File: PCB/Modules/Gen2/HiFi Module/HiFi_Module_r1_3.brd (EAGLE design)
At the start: 78.7 x 56.5 mm, 22 parts, among them IC1 SN65HVD31DR, IC2 ADUM5200ARWZ, T4_1 TEENSY4.1_FORAUDIO

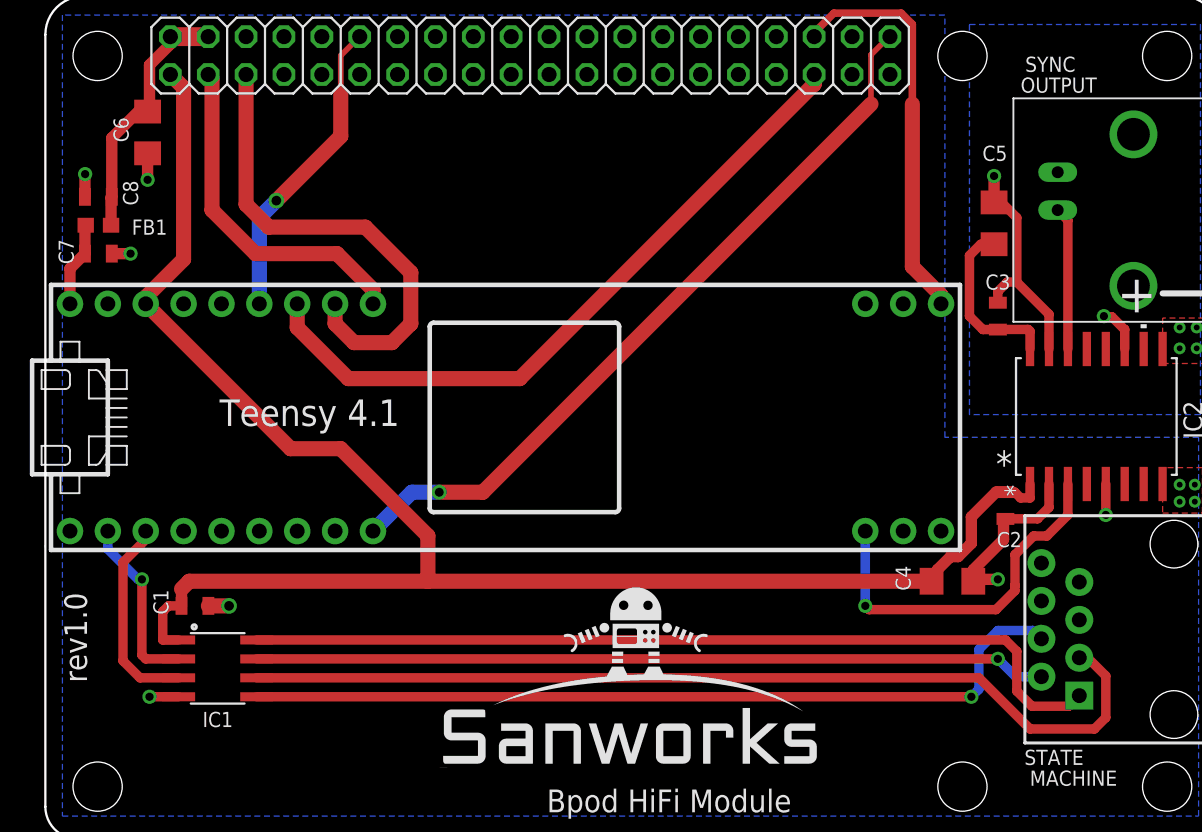
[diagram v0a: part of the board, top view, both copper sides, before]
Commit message: -Updated HiFi module PCB to v1.3. New version pulls unused channel to GND on ADUM5200 isolator, and contains silkscreen instructions for header mounting -Updated Raspberry Pi Shim to v1.1. New version provides more space between RJ45 jack and RS-485 IC for even mounting.
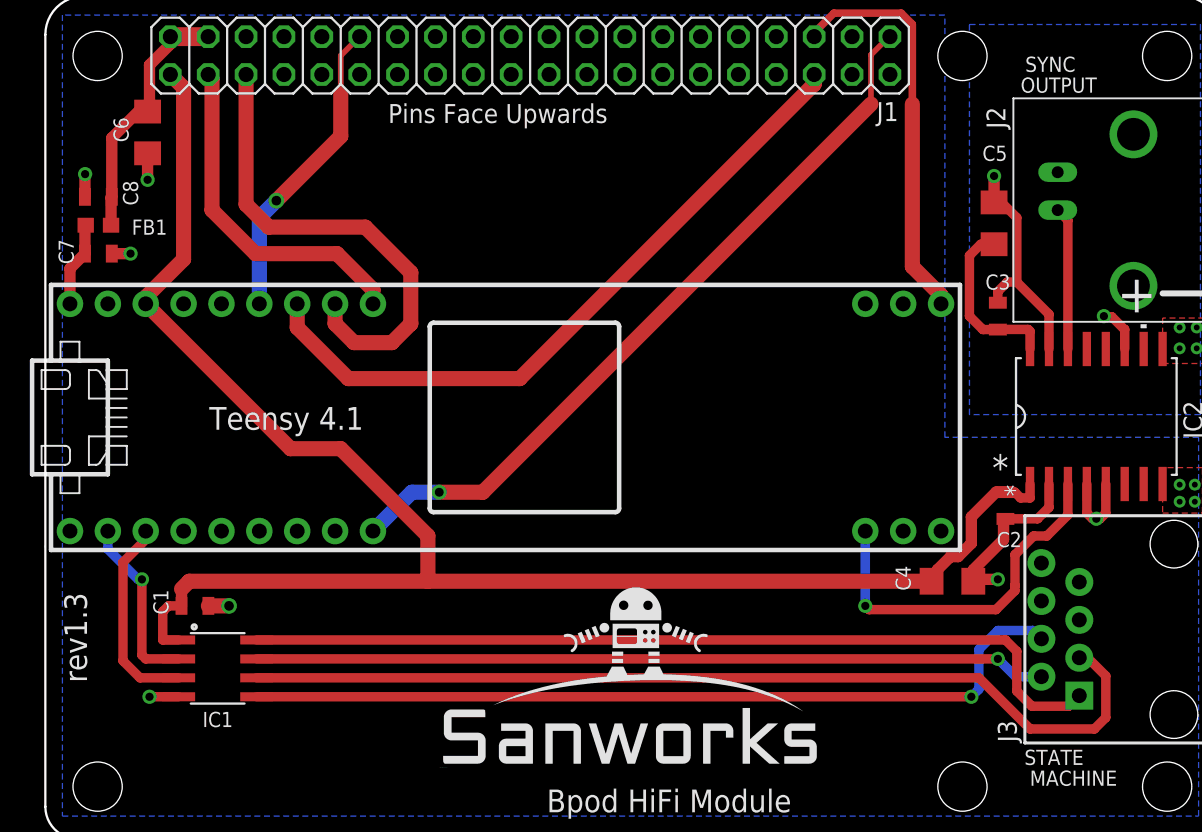
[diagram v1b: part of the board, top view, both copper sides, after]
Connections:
- net GND: now also IC2.4
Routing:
- net GND: track 21.6 -> 25.0 mm
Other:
- board text added: "J1"
- board text added: "J2"
- board text added: "J3"
- board text added: "Pins Face Upwards"
- board text added: "rev1.3"
- board text removed: "rev1.0"
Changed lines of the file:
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@@
 <wire x1="0" y1="19.558" x2="0" y2="19.685" width="0" layer="20"/>
 <text x="50.038" y="3.302" size="1.524" layer="21" font="vector" rot="R180">Bpod HiFi Module</text>
-<text x="1.27" y="16.51" size="1.524" layer="21" font="vector" rot="R270">rev1.0</text>
+<text x="1.27" y="16.51" size="1.524" layer="21" font="vector" rot="R270">rev1.3</text>
 <polygon width="1.016" layer="42">
 <vertex x="6.223" y="55.626"/>
@@
 <vertex x="77.851" y="55.499"/>
 </polygon>
-<text x="23.749" y="29.464" size="1.778" layer="21" font="vector" rot="R180">Teensy 4.1</text>
+<text x="21.336" y="28.956" size="1.524" layer="21" font="vector" rot="R180">Teensy 4.1</text>
 <text x="69.088" y="52.451" size="1.016" layer="21" font="vector" rot="R180">SYNC</text>
 <text x="65.405" y="50.038" size="1.016" layer="21" font="vector">OUTPUT</text>
-<text x="63.754" y="24.257" size="1.778" layer="21">*</text>
+<text x="63.5" y="24.003" size="1.778" layer="21">*</text>
+<text x="55.753" y="48.133" size="1.27" layer="21" font="vector">J1</text>
+<text x="64.389" y="47.625" size="1.27" layer="21" font="vector" rot="R90">J2</text>
+<text x="65.151" y="6.477" size="1.27" layer="21" font="vector" rot="R90">J3</text>
+<text x="22.987" y="48.006" size="1.27" layer="21" font="vector">Pins Face Upwards</text>
+<wire x1="65.151" y1="29.083" x2="65.151" y2="27.559" width="0.1524" layer="21" curve="-143.398488"/>
 </plain>
 <attributes>
@@
 <vertex x="60.325" y="55.245"/>
 </polygon>
-<via x="71.12" y="21.717" extent="1-16" drill="0.55"/>
-<wire x1="71.12" y1="23.79345" x2="71.12" y2="21.717" width="0.635" layer="1"/>
+<via x="70.485" y="21.463" extent="1-16" drill="0.55"/>
+<wire x1="71.12" y1="23.79345" x2="71.12" y2="21.844" width="0.635" layer="1"/>
+<wire x1="71.12" y1="21.844" x2="70.739" y2="21.463" width="0.635" layer="1"/>
+<wire x1="70.739" y1="21.463" x2="70.485" y2="21.463" width="0.635" layer="1"/>
 <wire x1="62.233" y1="17.272" x2="62.36" y2="17.399" width="0.762" layer="1"/>
 <wire x1="63.881" y1="17.399" x2="62.36" y2="17.399" width="0.762" layer="1"/>
@@
 <contactref element="T4_1" pad="22/A8"/>
 <contactref element="T4_1" pad="23/A9"/>
+<contactref element="IC2" pad="4"/>
+<wire x1="69.85" y1="23.79345" x2="69.85" y2="21.844" width="0.635" layer="1"/>
+<wire x1="70.485" y1="21.463" x2="70.231" y2="21.463" width="0.635" layer="1"/>
+<wire x1="70.231" y1="21.463" x2="69.85" y2="21.844" width="0.635" layer="1"/>
 </signal>
 <signal name="TXD">
